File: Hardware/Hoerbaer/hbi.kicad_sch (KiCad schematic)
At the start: 47 parts, among them J10 LEDS, J11 LEDS, J6 BUTTONS, J7 BUTTONS, J8 BUTTONS, J9 LEDS, U2 PCF8574TS, U3 PCF8574TS, U4 PCF8574TS, U5 TLC59108xPW, U6 TLC59108xPW, U7 TLC59108xPW

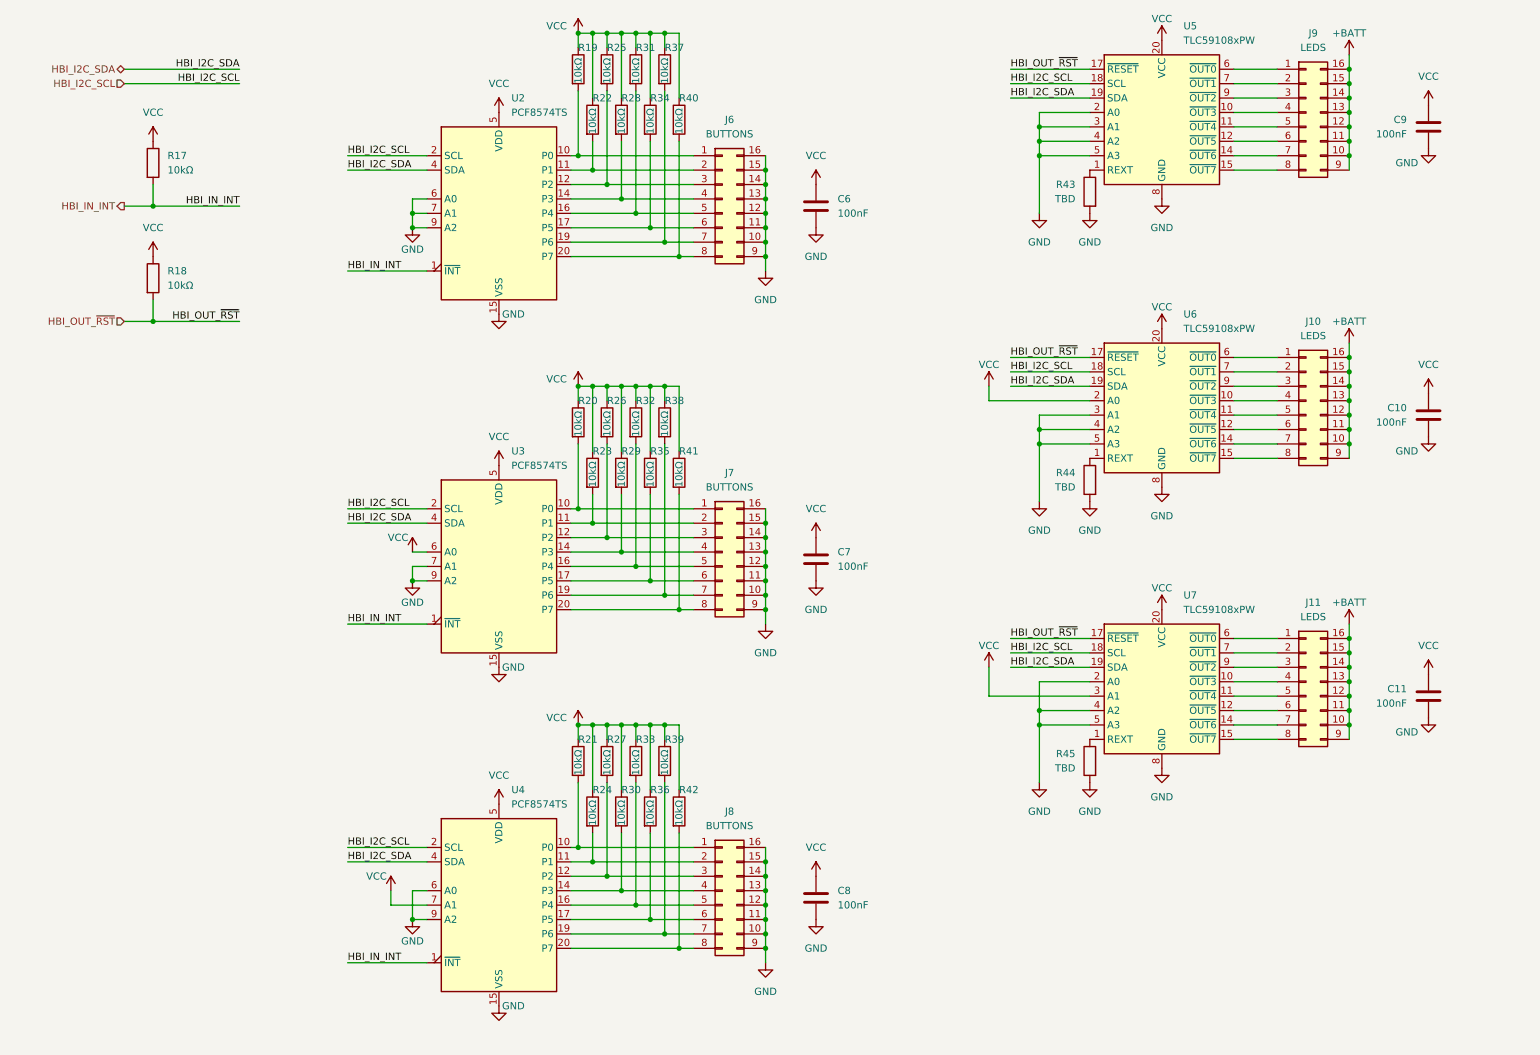
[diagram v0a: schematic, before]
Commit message: Nearly complete schematic with TLV61048 as 12V booster.
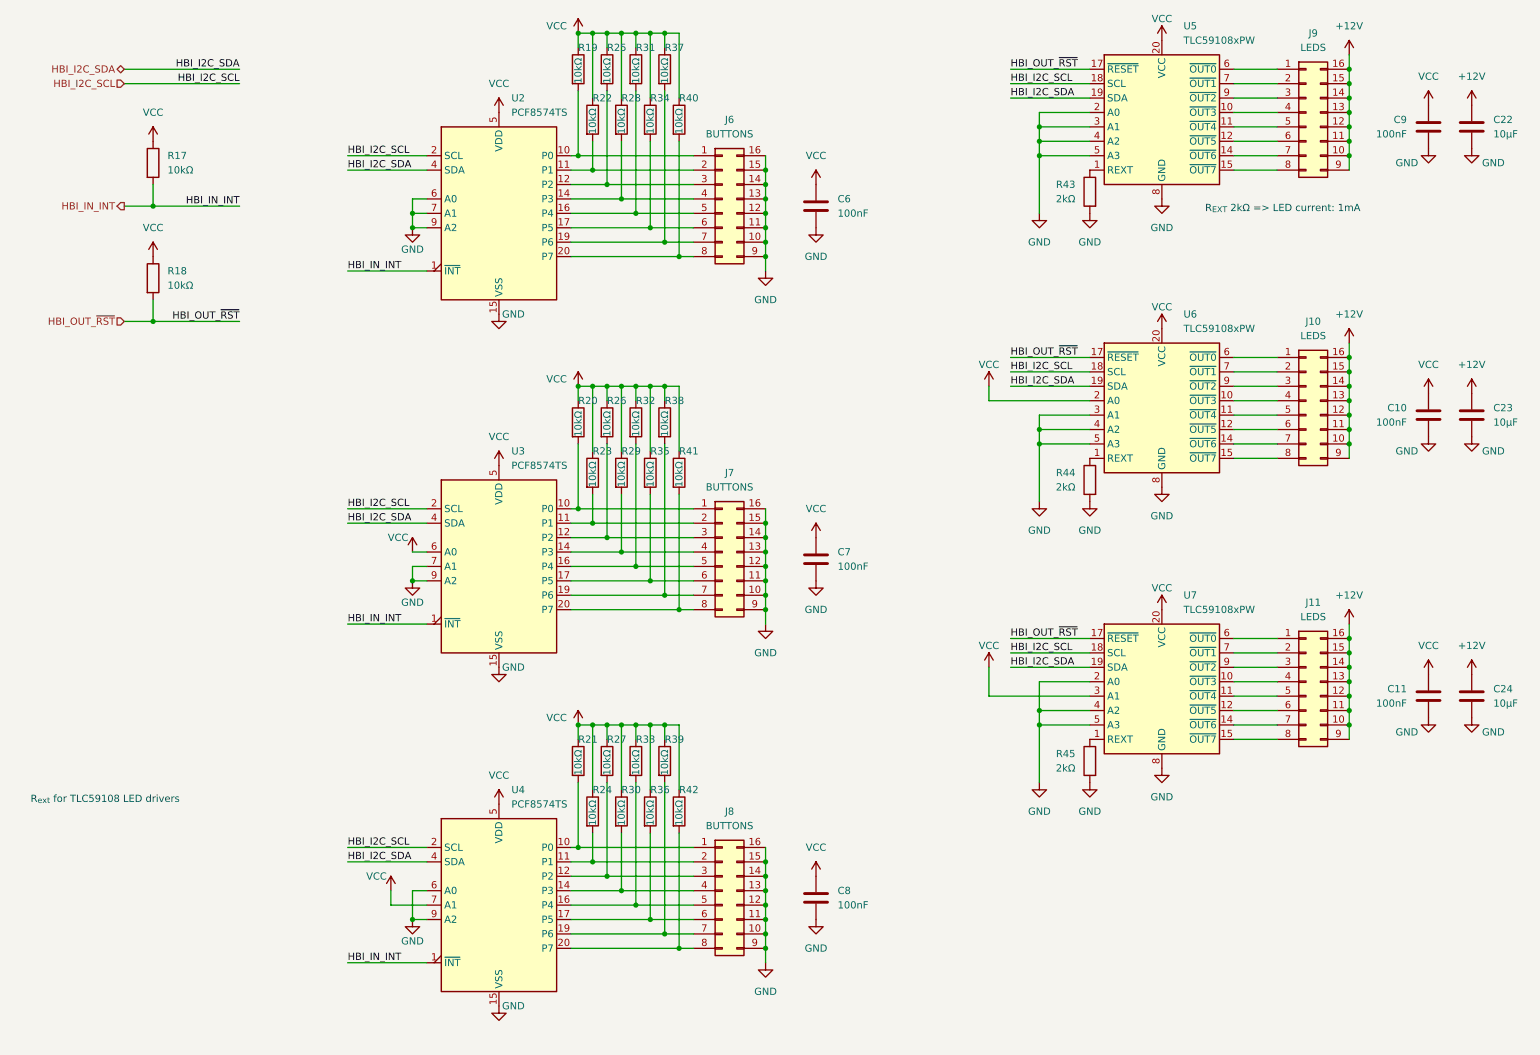
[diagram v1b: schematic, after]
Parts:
- added C22, C23, C24: 10µF, symbol Device:C
- R43, R44, R45: value TBD -> 2kΩ
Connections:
- net GND: now also C22.2, C23.2, C24.2
- net +BATT renamed +12V
- net +12V: now also C22.1, C23.1, C24.1
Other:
- note added: "R_{EXT} 2kΩ => LED current: 1mA"
- note added: "R_{ext} for TLC59108 LED drivers"
- company: (none) -> Drachosaurus Designs
- title: (none) -> Hör Bär main

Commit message: Footprints, order numbers, ...
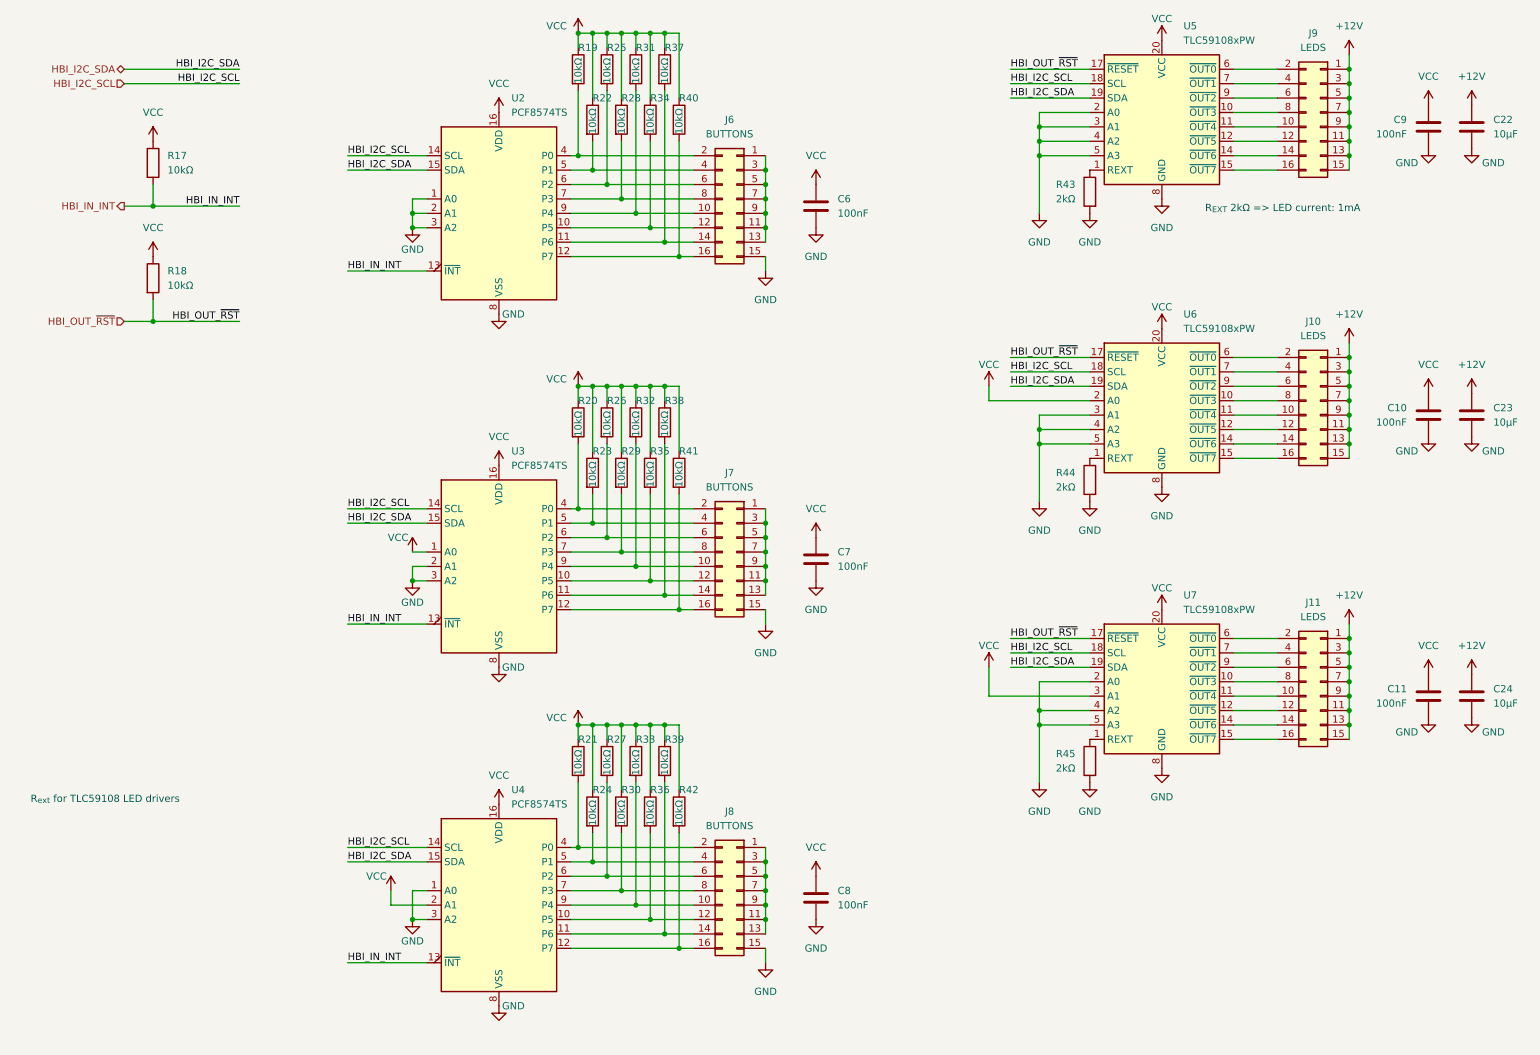
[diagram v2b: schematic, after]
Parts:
- C10, C11, C6, C7, C8, C9: footprint (none) -> Capacitor_SMD:C_0402_1005Metric
- C22, C23, C24: footprint (none) -> Capacitor_SMD:C_0805_2012Metric; JLCPCB (none) -> C6119932; MPN (none) -> CGA0805X7R106K250MT
- J10, J11, J6, J7, J8, J9: symbol Connector_Generic:Conn_02x08_Counter_Clockwise -> Connector_Generic:Conn_02x08_Odd_Even
- R17, R18, R19, R20, R21, R22, R23, R24, R25, R26, R27, R28, R29, R30, R31, R32, R33, R34, R35, R36, R37, R38, R39, R40, R41, R42, R43, R44, R45: footprint (none) -> Resistor_SMD:R_0402_1005Metric
- U2, U3, U4: footprint Package_SO:SSOP-20_4.4x6.5mm_P0.65mm -> Package_SO:SOIC-16W_7.5x10.3mm_P1.27mm; symbol Interface_Expansion:PCF8574TS -> Interface_Expansion:PCF8574A; JLCPCB (none) -> C2987289; MPN (none) -> PCF8574AT/TR
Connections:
- net +12V: now also J10.1 (Pin_1), J10.3 (Pin_3), J10.5 (Pin_5), J10.7 (Pin_7), J11.1 (Pin_1), J11.3 (Pin_3), J11.5 (Pin_5), J11.7 (Pin_7), J9.1 (Pin_1), J9.3 (Pin_3), J9.5 (Pin_5), J9.7 (Pin_7); no longer J10.10 (Pin_10), J10.12 (Pin_12), J10.14 (Pin_14), J10.16 (Pin_16), J11.10 (Pin_10), J11.12 (Pin_12), J11.14 (Pin_14), J11.16 (Pin_16), J9.10 (Pin_10), J9.12 (Pin_12), J9.14 (Pin_14), J9.16 (Pin_16)
- net GND: now also U2.1 (A0), U2.2 (A1), U2.3 (A2), U2.8 (VSS), U3.2 (A1), U3.3 (A2), U3.8 (VSS), U4.1 (A0), U4.3 (A2), U4.8 (VSS); no longer J6.10 (Pin_10), J6.11 (Pin_11), J6.12 (Pin_12), J6.13 (Pin_13), J6.14 (Pin_14), J6.16 (Pin_16), J6.9 (Pin_9), J7.10 (Pin_10), J7.11 (Pin_11), J7.12 (Pin_12), J7.13 (Pin_13), J7.14 (Pin_14), J7.16 (Pin_16), J7.9 (Pin_9), J8.10 (Pin_10), J8.11 (Pin_11), J8.12 (Pin_12), J8.13 (Pin_13), J8.14 (Pin_14), J8.16 (Pin_16), J8.9 (Pin_9), U2.15 (VSS), U2.6 (A0), U2.7 (A1), U2.9 (A2), U3.15 (VSS), U3.7 (A1), U3.9 (A2), U4.15 (VSS), U4.6 (A0), U4.9 (A2)
- net HBI_I2C_SCL: now also U2.14 (SCL), U3.14 (SCL), U4.14 (SCL); no longer U2.2 (SCL), U3.2 (SCL), U4.2 (SCL)
- net HBI_I2C_SDA: now also U2.15 (SDA), U3.15 (SDA), U4.15 (SDA); no longer U2.4 (SDA), U3.4 (SDA), U4.4 (SDA)
- net HBI_IN_INT: now also U2.13 (~{INT}), U3.13 (~{INT}), U4.13 (~{INT}); no longer U2.1 (~{INT}), U3.1 (~{INT}), U4.1 (~{INT})
- net VCC: now also U2.16 (VDD), U3.1 (A0), U3.16 (VDD), U4.16 (VDD), U4.2 (A1); no longer U2.5 (VDD), U3.5 (VDD), U3.6 (A0), U4.5 (VDD), U4.7 (A1)
- net at U7.10 (~{OUT3}): now also J11.8 (Pin_8); no longer J11.4 (Pin_4)
- net at U7.11 (~{OUT4}): now also J11.10 (Pin_10); no longer J11.5 (Pin_5)
- net at U7.12 (~{OUT5}): now also J11.12 (Pin_12); no longer J11.6 (Pin_6)
- net at U7.14 (~{OUT6}): now also J11.14 (Pin_14); no longer J11.7 (Pin_7)
- net at U7.15 (~{OUT7}): now also J11.16 (Pin_16); no longer J11.8 (Pin_8)
- net at U7.6 (~{OUT0}): now also J11.2 (Pin_2); no longer J11.1 (Pin_1)
- net at U7.7 (~{OUT1}): now also J11.4 (Pin_4); no longer J11.2 (Pin_2)
- net at U7.9 (~{OUT2}): now also J11.6 (Pin_6); no longer J11.3 (Pin_3)
- net at U5.10 (~{OUT3}): now also J9.8 (Pin_8); no longer J9.4 (Pin_4)
- net at U5.11 (~{OUT4}): now also J9.10 (Pin_10); no longer J9.5 (Pin_5)
- net at U5.12 (~{OUT5}): now also J9.12 (Pin_12); no longer J9.6 (Pin_6)
- net at U5.14 (~{OUT6}): now also J9.14 (Pin_14); no longer J9.7 (Pin_7)
- net at U5.15 (~{OUT7}): now also J9.16 (Pin_16); no longer J9.8 (Pin_8)
- net at U5.6 (~{OUT0}): now also J9.2 (Pin_2); no longer J9.1 (Pin_1)
- net at U5.7 (~{OUT1}): now also J9.4 (Pin_4); no longer J9.2 (Pin_2)
- net at U5.9 (~{OUT2}): now also J9.6 (Pin_6); no longer J9.3 (Pin_3)
- net at U6.10 (~{OUT3}): now also J10.8 (Pin_8); no longer J10.4 (Pin_4)
- net at U6.11 (~{OUT4}): now also J10.10 (Pin_10); no longer J10.5 (Pin_5)
- net at U6.12 (~{OUT5}): now also J10.12 (Pin_12); no longer J10.6 (Pin_6)
- net at U6.14 (~{OUT6}): now also J10.14 (Pin_14); no longer J10.7 (Pin_7)
- net at U6.15 (~{OUT7}): now also J10.16 (Pin_16); no longer J10.8 (Pin_8)
- net at U6.6 (~{OUT0}): now also J10.2 (Pin_2); no longer J10.1 (Pin_1)
- net at U6.7 (~{OUT1}): now also J10.4 (Pin_4); no longer J10.2 (Pin_2)
- net at U6.9 (~{OUT2}): now also J10.6 (Pin_6); no longer J10.3 (Pin_3)
- new net: J8.4 (Pin_4), R24.2, U4.5 (P1)
- new net: J6.2 (Pin_2), R19.2, U2.4 (P0)
- new net: J7.8 (Pin_8), R29.2, U3.7 (P3)
- new net: J8.12 (Pin_12), R36.2, U4.10 (P5)
- new net: J8.14 (Pin_14), R39.2, U4.11 (P6)
- new net: J8.16 (Pin_16), R42.2, U4.12 (P7)
- new net: J8.2 (Pin_2), R21.2, U4.4 (P0)
- new net: J8.6 (Pin_6), R27.2, U4.6 (P2)
- new net: J8.8 (Pin_8), R30.2, U4.7 (P3)
- new net: J8.10 (Pin_10), R33.2, U4.9 (P4)
- new net: J7.12 (Pin_12), R35.2, U3.10 (P5)
- new net: J7.14 (Pin_14), R38.2, U3.11 (P6)
- new net: J7.16 (Pin_16), R41.2, U3.12 (P7)
- new net: J7.2 (Pin_2), R20.2, U3.4 (P0)
- new net: J7.4 (Pin_4), R23.2, U3.5 (P1)
- new net: J7.6 (Pin_6), R26.2, U3.6 (P2)
- new net: J7.10 (Pin_10), R32.2, U3.9 (P4)
- new net: J7.1 (Pin_1), J7.11 (Pin_11), J7.13 (Pin_13), J7.3 (Pin_3), J7.5 (Pin_5), J7.7 (Pin_7), J7.9 (Pin_9)
- new net: J6.6 (Pin_6), R25.2, U2.6 (P2)
- new net: J6.12 (Pin_12), R34.2, U2.10 (P5)
- new net: J6.1 (Pin_1), J6.11 (Pin_11), J6.13 (Pin_13), J6.3 (Pin_3), J6.5 (Pin_5), J6.7 (Pin_7), J6.9 (Pin_9)
- new net: J6.10 (Pin_10), R31.2, U2.9 (P4)
- new net: J6.14 (Pin_14), R37.2, U2.11 (P6)
- new net: J6.16 (Pin_16), R40.2, U2.12 (P7)
- new net: J6.4 (Pin_4), R22.2, U2.5 (P1)
- new net: J6.8 (Pin_8), R28.2, U2.7 (P3)
- new net: J8.1 (Pin_1), J8.11 (Pin_11), J8.13 (Pin_13), J8.3 (Pin_3), J8.5 (Pin_5), J8.7 (Pin_7), J8.9 (Pin_9)
